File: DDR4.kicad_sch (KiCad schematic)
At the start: 39 parts, among them U14 2199155-1

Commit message: Update PCB naming
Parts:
- C153, C154, C160, C161, C162, C163, C164, C165, C166, C167, C168, C169, C170, C171, C173, C176, C177, C179, C181, C199, C200, C201, C202, C203, C204, C205, C208, C209, C210, C211, C212, C213, C214: footprint data-center-dram-tester-footprints:0402-cap -> data-center-rdimm-ddr4-tester-footprints:0402-cap; symbol data-center-dram-tester:C_100n_0402 -> data-center-rdimm-ddr4-tester:C_100n_0402
- R157, R158, R185: footprint data-center-dram-tester-footprints:0402-res -> data-center-rdimm-ddr4-tester-footprints:0402-res; symbol data-center-dram-tester:R_0R_0402 -> data-center-rdimm-ddr4-tester:R_0R_0402
- R186: footprint data-center-dram-tester-footprints:0402-res -> data-center-rdimm-ddr4-tester-footprints:0402-res; symbol data-center-dram-tester:R_100k_0402 -> data-center-rdimm-ddr4-tester:R_100k_0402
- TP10: footprint data-center-dram-tester-footprints:Testpoint_smd_1mm -> data-center-rdimm-ddr4-tester-footprints:Testpoint_smd_1mm; symbol data-center-dram-tester:TP_SMD1MM -> data-center-rdimm-ddr4-tester:TP_SMD1MM
- U14: footprint data-center-dram-tester-footprints:2199155-1 -> data-center-rdimm-ddr4-tester-footprints:2199155-1; symbol data-center-dram-tester:2199155-1 -> data-center-rdimm-ddr4-tester:2199155-1
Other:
- title: Data Center DRAM Tester -> Data Center RDIMM DDR4 Tester

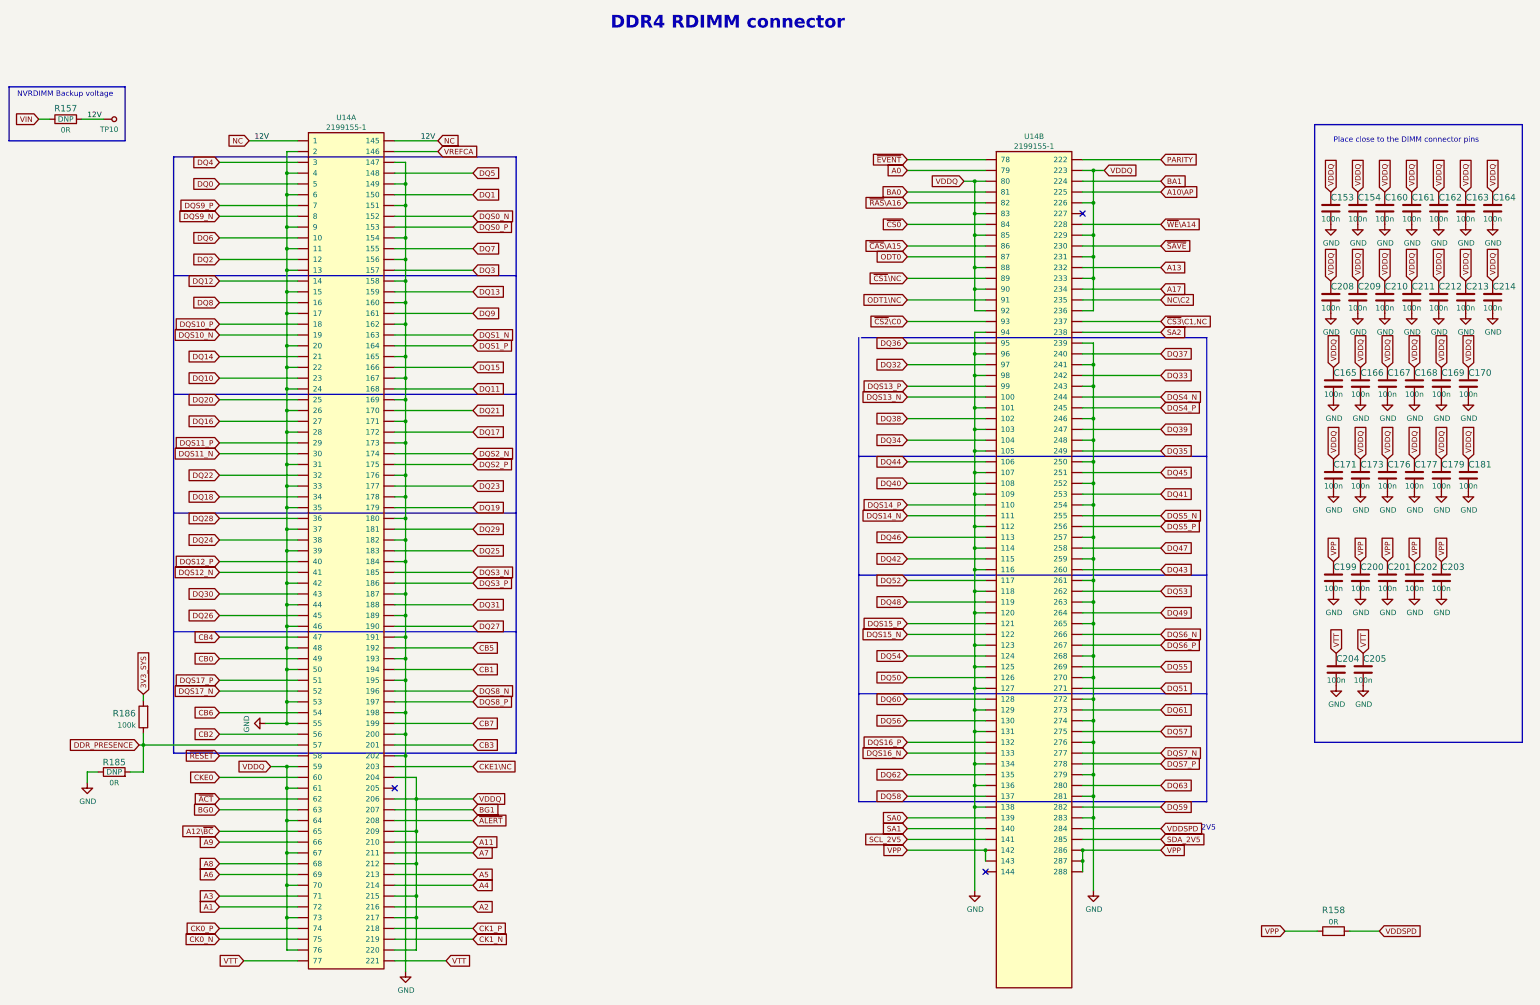
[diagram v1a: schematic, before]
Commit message: Introduce component standardization
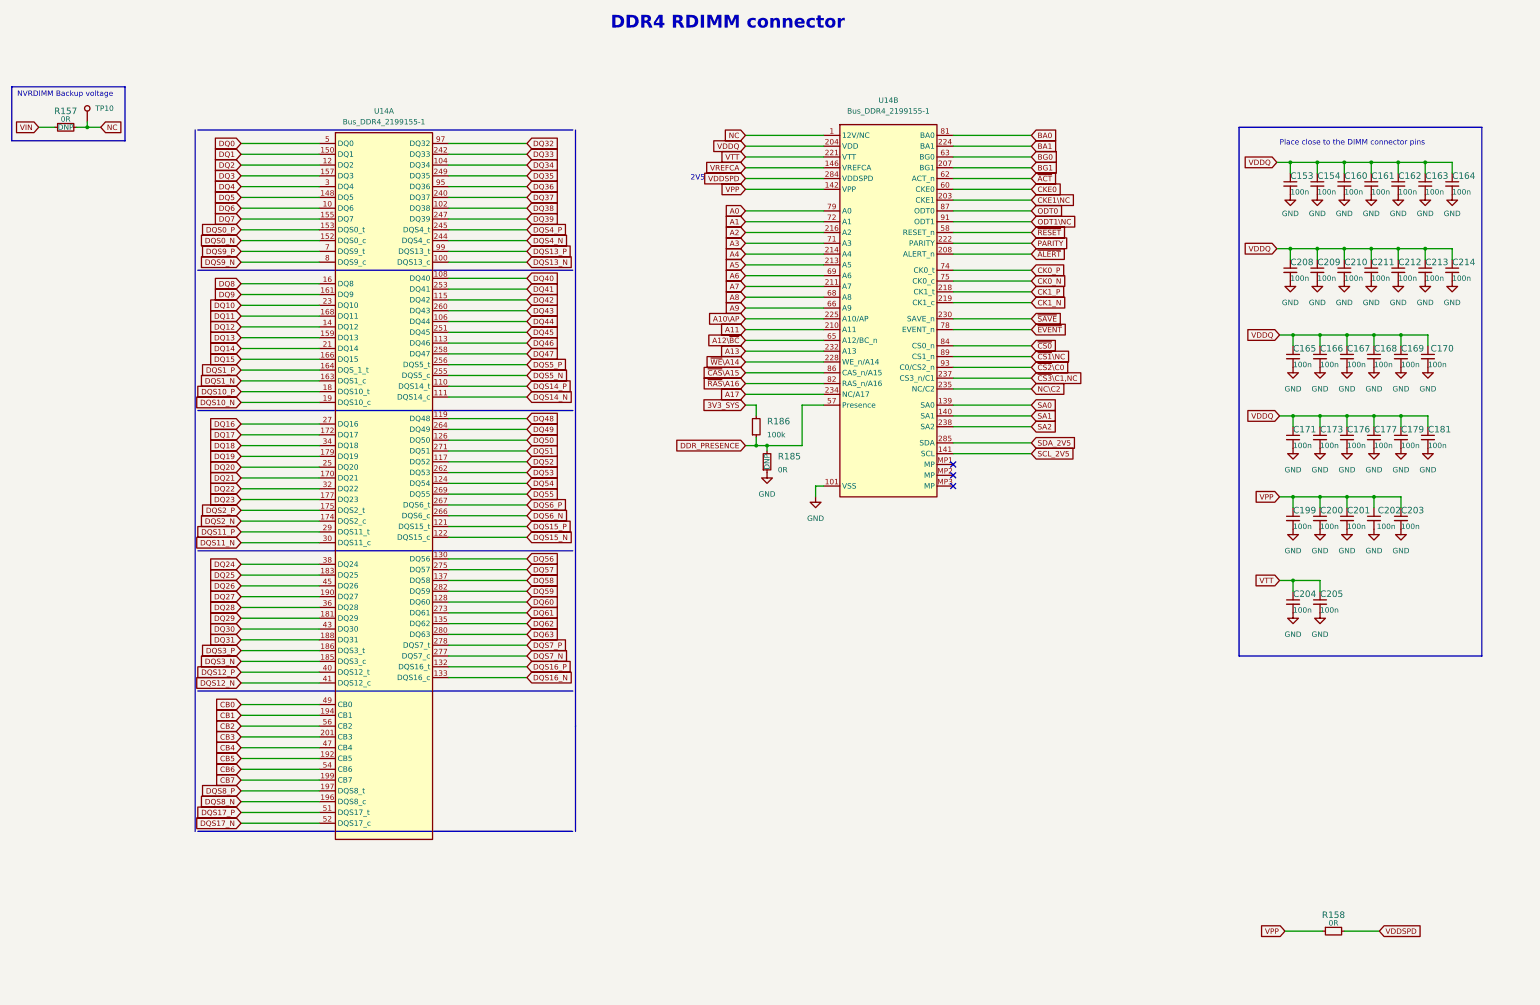
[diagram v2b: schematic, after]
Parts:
- C153, C154, C160, C161, C162, C163, C164, C165, C166, C167, C168, C169, C170, C171, C173, C176, C177, C179, C181, C199, C200, C201, C202, C203, C204, C205, C208, C209, C210, C211, C212, C213, C214: footprint data-center-rdimm-ddr4-tester-footprints:0402-cap -> data-center-rdimm-ddr4-tester-footprints:C_0402_1005Metric; Author (none) -> Antmicro; Dielectric (none) -> X5R; License (none) -> Apache-2.0; Voltage (none) -> 50V
- R157, R158, R185: footprint data-center-rdimm-ddr4-tester-footprints:0402-res -> data-center-rdimm-ddr4-tester-footprints:R_0402_1005Metric; Author (none) -> Antmicro; Current (none) -> 1A; License (none) -> Apache-2.0; Manufacturer PANASONIC -> Panasonic
- R186: footprint data-center-rdimm-ddr4-tester-footprints:0402-res -> data-center-rdimm-ddr4-tester-footprints:R_0402_1005Metric; Author (none) -> Antmicro; License (none) -> Apache-2.0; MPN CRCW0402100KFKEDHP -> CR0402-FX-1003GLF; Manufacturer VISHAY -> Bourns; Tolerance (none) -> 1%
- TP10: value TP_SMD1MM -> TP_1mm_SMD; symbol data-center-rdimm-ddr4-tester:TP_SMD1MM -> data-center-rdimm-ddr4-tester:TP_1mm_SMD; Author (none) -> Antmicro; License (none) -> Apache-2.0
- U14: value 2199155-1 -> Bus_DDR4_2199155-1; footprint data-center-rdimm-ddr4-tester-footprints:2199155-1 -> data-center-rdimm-ddr4-tester-footprints:Bus_DDR4_Socket_DIMM_2199155-1; symbol data-center-rdimm-ddr4-tester:2199155-1 -> data-center-rdimm-ddr4-tester:Bus_DDR4_2199155-1; Author (none) -> Antmicro; License (none) -> Apache-2.0; MPN (none) -> 2199155-1; Manufacturer (none) -> TE Connectivity
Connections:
- net A1: now also U14.72 (A1); no longer U14.72
- net A11: now also U14.210 (A11); no longer U14.210
- net A12\~{BC}: now also U14.65 (A12/BC_n); no longer U14.65
- net A2: now also U14.216 (A2); no longer U14.216
- net A3: now also U14.71 (A3); no longer U14.71
- net A4: now also U14.214 (A4); no longer U14.214
- net A5: now also U14.213 (A5); no longer U14.213
- net A6: now also U14.69 (A6); no longer U14.69
- net A7: now also U14.211 (A7); no longer U14.211
- net A8: now also U14.68 (A8); no longer U14.68
- net A9: now also U14.66 (A9); no longer U14.66
- net BG0: now also U14.63 (BG0); no longer U14.63
- net BG1: now also U14.207 (BG1); no longer U14.207
- net CK0_N: now also U14.75 (CK0_c); no longer U14.75
- net CK0_P: now also U14.74 (CK0_t); no longer U14.74
- net CK1_N: now also U14.219 (CK1_c); no longer U14.219
- net CK1_P: now also U14.218 (CK1_t); no longer U14.218
- net CKE0: now also U14.60 (CKE0); no longer U14.60
- net CKE1\NC: now also U14.203 (CKE1); no longer U14.203
- net DDR_PRESENCE: now also U14.57 (Presence); no longer U14.57
- net DQ32: now also U14.97 (DQ32); no longer U14.97
- net DQ33: now also U14.242 (DQ33); no longer U14.242
- net DQ34: now also U14.104 (DQ34); no longer U14.104
- net DQ35: now also U14.249 (DQ35); no longer U14.249
- net DQ36: now also U14.95 (DQ36); no longer U14.95
- net DQ37: now also U14.240 (DQ37); no longer U14.240
- net DQ38: now also U14.102 (DQ38); no longer U14.102
- net DQ39: now also U14.247 (DQ39); no longer U14.247
- net DQ40: now also U14.108 (DQ40); no longer U14.108
- net DQ41: now also U14.253 (DQ41); no longer U14.253
- net DQ42: now also U14.115 (DQ42); no longer U14.115
- net DQ43: now also U14.260 (DQ43); no longer U14.260
- net DQ44: now also U14.106 (DQ44); no longer U14.106
- net DQ45: now also U14.251 (DQ45); no longer U14.251
- net DQ46: now also U14.113 (DQ46); no longer U14.113
- net DQ47: now also U14.258 (DQ47); no longer U14.258
- net DQ48: now also U14.119 (DQ48); no longer U14.119
- net DQ49: now also U14.264 (DQ49); no longer U14.264
- net DQ50: now also U14.126 (DQ50); no longer U14.126
- net DQ51: now also U14.271 (DQ51); no longer U14.271
- net DQ52: now also U14.117 (DQ52); no longer U14.117
- net DQ53: now also U14.262 (DQ53); no longer U14.262
- net DQ54: now also U14.124 (DQ54); no longer U14.124
- net DQ55: now also U14.269 (DQ55); no longer U14.269
- net DQ56: now also U14.130 (DQ56); no longer U14.130
- net DQ57: now also U14.275 (DQ57); no longer U14.275
- net DQ58: now also U14.137 (DQ58); no longer U14.137
- net DQ59: now also U14.282 (DQ59); no longer U14.282
- net DQ60: now also U14.128 (DQ60); no longer U14.128
- net DQ61: now also U14.273 (DQ61); no longer U14.273
- net DQ62: now also U14.135 (DQ62); no longer U14.135
- net DQ63: now also U14.280 (DQ63); no longer U14.280
- net DQS13_N: now also U14.100 (DQS13_c); no longer U14.100
- net DQS13_P: now also U14.99 (DQS13_t); no longer U14.99
- net DQS14_N: now also U14.111 (DQS14_c); no longer U14.111
- net DQS14_P: now also U14.110 (DQS14_t); no longer U14.110
- net DQS15_N: now also U14.122 (DQS15_c); no longer U14.122
- net DQS15_P: now also U14.121 (DQS15_t); no longer U14.121
- net DQS16_N: now also U14.133 (DQS16_c); no longer U14.133
- net DQS16_P: now also U14.132 (DQS16_t); no longer U14.132
- net DQS4_N: now also U14.244 (DQS4_c); no longer U14.244
- net DQS4_P: now also U14.245 (DQS4_t); no longer U14.245
- net DQS5_N: now also U14.255 (DQS5_c); no longer U14.255
- net DQS5_P: now also U14.256 (DQS5_t); no longer U14.256
- net DQS6_N: now also U14.266 (DQS6_c); no longer U14.266
- net DQS6_P: now also U14.267 (DQS6_t); no longer U14.267
- net DQS7_N: now also U14.277 (DQS7_c); no longer U14.277
- net DQS7_P: now also U14.278 (DQS7_t); no longer U14.278
- net GND: now also U14.11 (VSS), U14.13 (VSS), U14.147 (VSS), U14.149 (VSS), U14.15 (VSS), U14.151 (VSS), U14.154 (VSS), U14.156 (VSS), U14.158 (VSS), U14.160 (VSS), U14.162 (VSS), U14.165 (VSS), U14.167 (VSS), U14.169 (VSS), U14.17 (VSS), U14.171 (VSS), U14.173 (VSS), U14.176 (VSS), U14.178 (VSS), U14.180 (VSS), U14.182 (VSS), U14.184 (VSS), U14.187 (VSS), U14.189 (VSS), U14.191 (VSS), U14.193 (VSS), U14.195 (VSS), U14.198 (VSS), U14.2 (VSS), U14.20 (VSS), U14.200 (VSS), U14.202 (VSS), U14.22 (VSS), U14.24 (VSS), U14.26 (VSS), U14.28 (VSS), U14.31 (VSS), U14.33 (VSS), U14.35 (VSS), U14.37 (VSS), U14.39 (VSS), U14.4 (VSS), U14.42 (VSS), U14.44 (VSS), U14.46 (VSS), U14.48 (VSS), U14.50 (VSS), U14.53 (VSS), U14.55 (VSS), U14.6 (VSS), U14.9 (VSS); no longer U14.11, U14.13, U14.147, U14.149, U14.15, U14.151, U14.154, U14.156, U14.158, U14.160, U14.162, U14.165, U14.167, U14.169, U14.17, U14.171, U14.173, U14.176, U14.178, U14.180, U14.182, U14.184, U14.187, U14.189, U14.191, U14.193, U14.195, U14.198, U14.2, U14.20, U14.200, U14.202, U14.22, U14.24, U14.26, U14.28, U14.31, U14.33, U14.35, U14.37, U14.39, U14.4, U14.42, U14.44, U14.46, U14.48, U14.50, U14.53, U14.55, U14.6, U14.9
- net NC: now also U14.1 (12V/NC), U14.145 (12V/NC); no longer U14.1, U14.145
- net VDDQ: now also U14.204 (VDD), U14.206 (VDD), U14.209 (VDD), U14.212 (VDD), U14.215 (VDD), U14.217 (VDD), U14.220 (VDD), U14.59 (VDD), U14.61 (VDD), U14.64 (VDD), U14.67 (VDD), U14.70 (VDD), U14.73 (VDD), U14.76 (VDD); no longer U14.204, U14.206, U14.209, U14.212, U14.215, U14.217, U14.220, U14.59, U14.61, U14.64, U14.67, U14.70, U14.73, U14.76
- net VREFCA: now also U14.146 (VREFCA); no longer U14.146
- net VTT: now also U14.221 (VTT), U14.77 (VTT); no longer U14.221, U14.77
- net ~{ACT}: now also U14.62 (ACT_n); no longer U14.62
- net ~{ALERT}: now also U14.208 (ALERT_n); no longer U14.208
- net ~{RESET}: now also U14.58 (RESET_n); no longer U14.58
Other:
- moved on the sheet: C153, C154, C160, C161, C162, C163, C164, C165, C166, C167, C168, C169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

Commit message: [#55119] component update
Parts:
- C153, C154, C160, C161, C162, C163, C164, C165, C166, C167, C168, C169, C170, C171, C173, C176, C177, C179, C181, C199, C200, C201, C202, C203, C204, C205, C208, C209, C210, C211, C212, C213, C214: footprint data-center-rdimm-ddr4-tester-footprints:C_0402_1005Metric -> antmicro-footprints:C_0402_1005Metric; symbol data-center-rdimm-ddr4-tester:C_100n_0402 -> antmicroCapacitors0402:C_100n_0402
- R157, R185: footprint data-center-rdimm-ddr4-tester-footprints:R_0402_1005Metric -> antmicro-footprints:R_0402_1005Metric; symbol data-center-rdimm-ddr4-tester:R_0R_0402 -> antmicroResistors0402:R_0R_0402; now not fitted; now left out of the parts list
- R158: footprint data-center-rdimm-ddr4-tester-footprints:R_0402_1005Metric -> antmicro-footprints:R_0402_1005Metric; symbol data-center-rdimm-ddr4-tester:R_0R_0402 -> antmicroResistors0402:R_0R_0402
- R186: footprint data-center-rdimm-ddr4-tester-footprints:R_0402_1005Metric -> antmicro-footprints:R_0402_1005Metric; symbol data-center-rdimm-ddr4-tester:R_100k_0402 -> antmicroResistors0402:R_100k_0402
- TP10: footprint data-center-rdimm-ddr4-tester-footprints:Testpoint_smd_1mm -> antmicro-footprints:TP_SMD_1mm; symbol data-center-rdimm-ddr4-tester:TP_1mm_SMD -> antmicroTestPoints:TP_1mm_SMD
- U14: footprint data-center-rdimm-ddr4-tester-footprints:Bus_DDR4_Socket_DIMM_2199155-1 -> antmicro-footprints:Bus_DDR4_Socket_DIMM_2199155-1; symbol data-center-rdimm-ddr4-tester:Bus_DDR4_2199155-1 -> antmicroMemoryConnectorsPCCardSockets:Bus_DDR4_2199155-1
